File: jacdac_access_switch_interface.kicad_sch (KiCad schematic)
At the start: 23 parts

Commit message: v1.3 started, board outline complete
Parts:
- removed U: (no value), symbol Jacdac:jacdac_hole_GND_MH2A
- removed U: (no value), symbol Jacdac:jacdac_hole_GND_MH2B
- removed U: (no value), symbol Device:R
- added MH: jacdac_hole_GND_MH2, KittenBot:jacdac_hole_GND2, symbol Jacdac:jacdac_hole_GND_MH2
- added MH: jacdac_hole_GND_MH4, Kittenbot_Connector_Jacdac:jacdac_hole_GNDB, symbol Jacdac:jacdac_hole_GND_MH4
- added U (x2): (no value), symbol Device:R
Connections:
- net GND: now also MH.MH2A, MH.MH2B
- net at U.1: now also U.1
- net SWITCH renamed SWITCH1
- net SWITCH1: now also U.2
- new net: U.1, U.2
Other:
- moved on the sheet: U

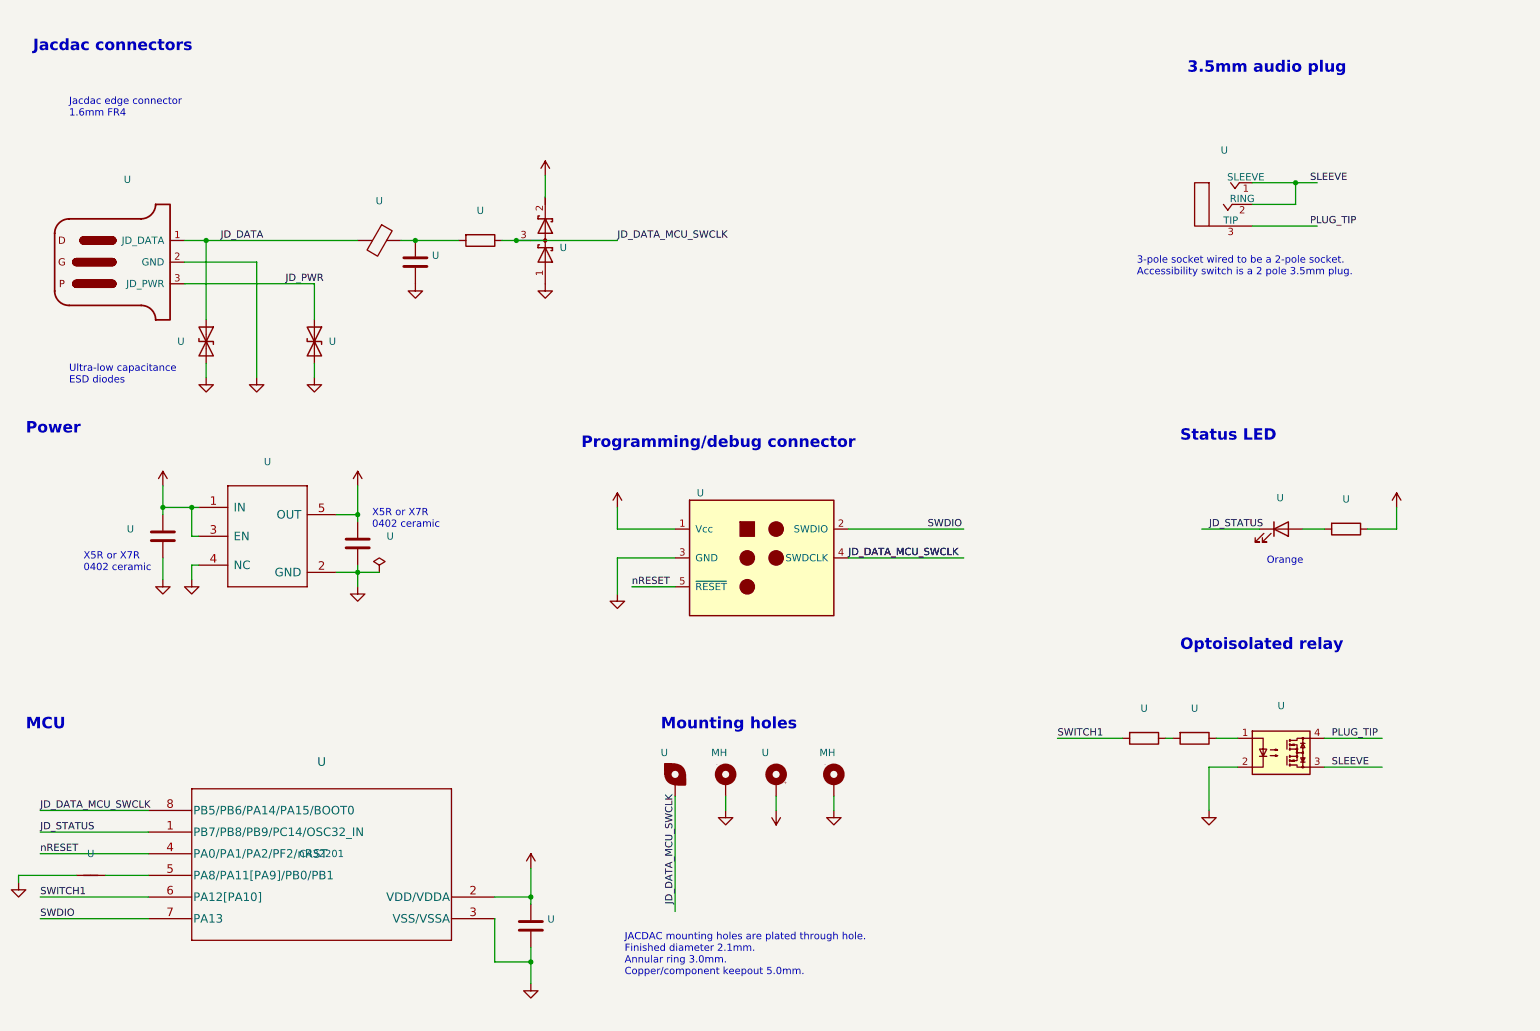
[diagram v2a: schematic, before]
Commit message: Replaced 3.5mm plug with 2x3.5mm sockets on schematic
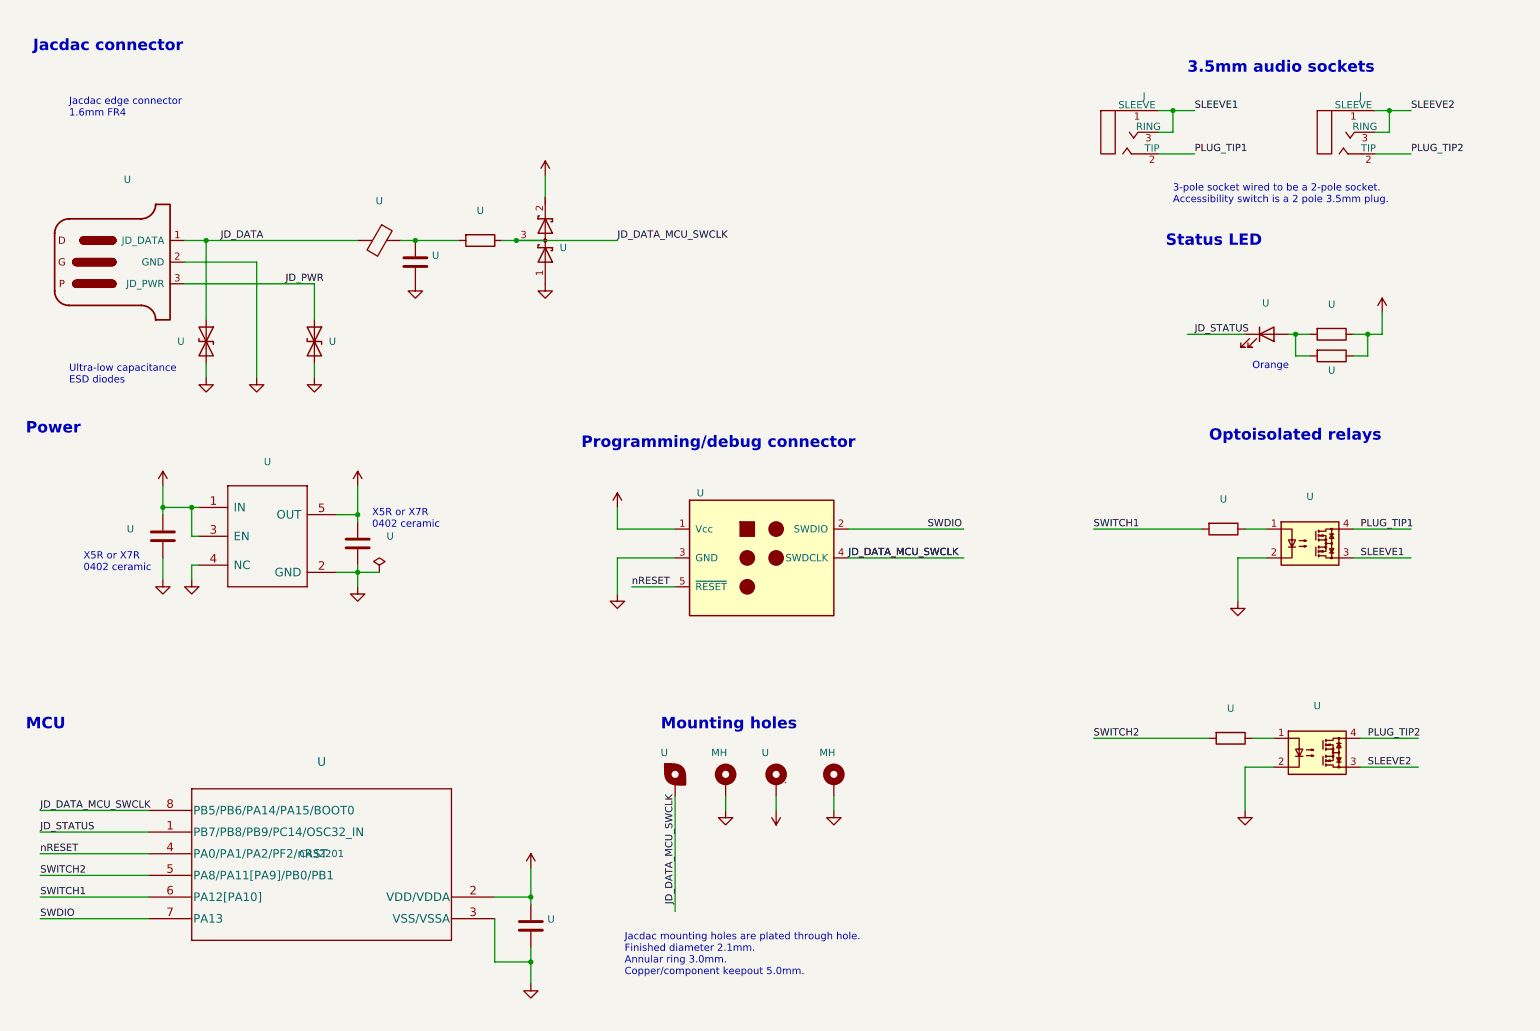
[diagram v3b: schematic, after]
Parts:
- removed U: (no value), symbol jacdac_access_switch_interface:54-00036_audio_plug
- removed U: (no value), symbol Device:NetTie_2
- removed U: (no value), symbol Device:R
- added J (x2): jack_3.5_pj313d, jacdac_access_switch_interface:jack_3.5_pj313d_smt, symbol jacdac_access_switch_interface:jack_3.5_pj313d
- added U (x2): (no value), symbol Device:R
- added U: (no value), symbol jacdac_access_switch_interface:AQY282
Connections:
- net +3V3: now also U.1
- net GND: now also U.2
- net SWITCH1: now also U.2
- net at U.2, U.2 (A): now also U.2
- net SWITCH2: now reaches U.5 (PA8/PA11[PA9]/PB0/PB1)
- net SWITCH2: now also U.2
- net PLUG_TIP renamed PLUG_TIP1
- net PLUG_TIP1: now also J.2 (TIP)
- net SLEEVE renamed SLEEVE1
- net SLEEVE1: now also J.1 (SLEEVE), J.3 (RING)
- new net: U.1, U.1
- new net PLUG_TIP2: J.2 (TIP), U.4
- new net SLEEVE2: J.1 (SLEEVE), J.3 (RING), U.3
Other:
- note added: "3.5mm audio sockets"
- note added: "Jacdac connector"
- note added: "Jacdac mounting holes are plated through hole. Finished diameter 2.1mm. Annular ring 3.0mm. Copper/component keepout 5.0mm."
- note added: "Optoisolated relays"
- note removed: "3.5mm audio plug"
- note removed: "JACDAC mounting holes are plated through hole. Finished diameter 2.1mm. Annular ring 3.0mm. Copper/component keepout 5.0mm."
- note removed: "Jacdac connectors"
- note removed: "Optoisolated relay"
- moved on the sheet: U

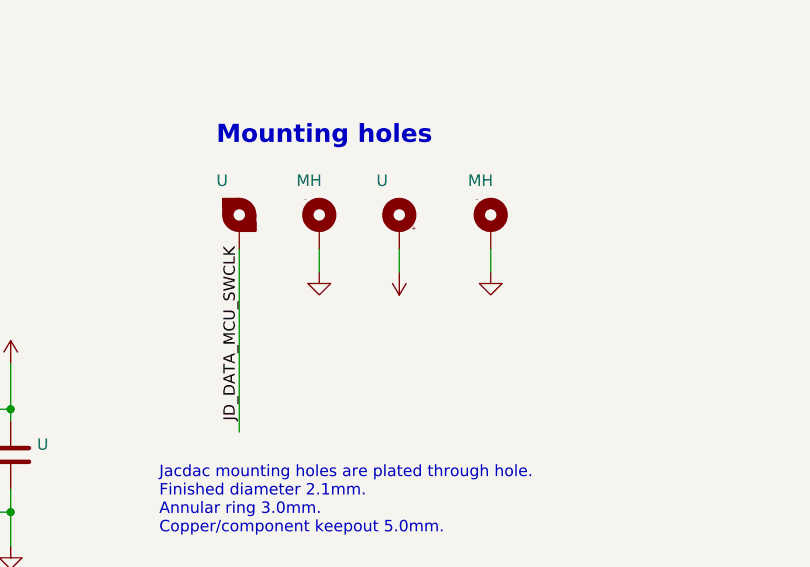
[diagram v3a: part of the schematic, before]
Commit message: Component placement for 30x30 board
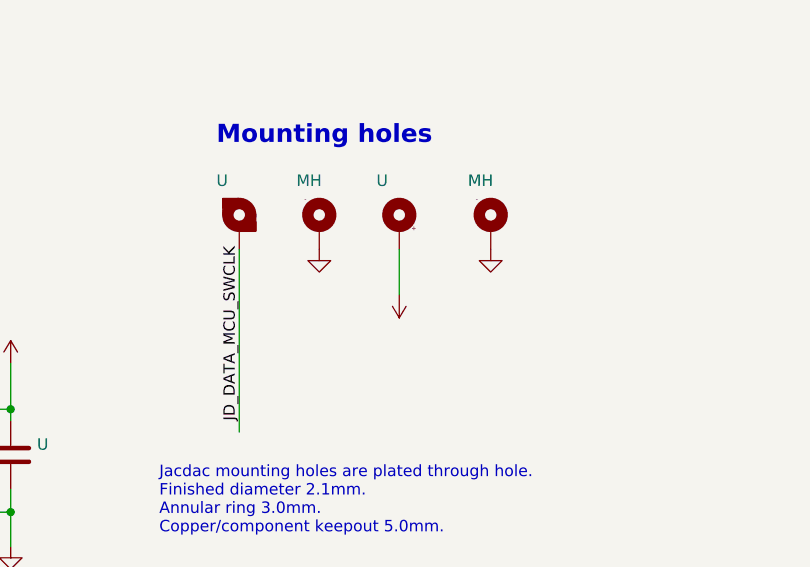
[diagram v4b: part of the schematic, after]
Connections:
- net GND: now also MH.MH2, MH.MH4; no longer MH.MH2A, MH.MH2B
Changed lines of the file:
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@@
-    (stroke (width 0) (type default))
-  )
-  (wire (pts (xy 139.7 151.13) (xy 139.7 153.67))
     (stroke (width 0) (type default))
   )
@@
     (stroke (width 0) (type default))
   )
+  (wire (pts (xy 148.59 151.13) (xy 148.59 156.21))
+    (stroke (width 0) (type default))
+  )
   (wire (pts (xy 256.54 30.48) (xy 256.54 34.29))
     (stroke (width 0) (type default))
@@
     (stroke (width 0) (type default))
   )
-  (wire (pts (xy 148.59 151.13) (xy 148.59 153.67))
-    (stroke (width 0) (type default))
-  )
   (wire (pts (xy 44.45 57.15) (xy 57.15 57.15))
     (stroke (width 0) (type default))
@@
   )
   (wire (pts (xy 46.99 105.41) (xy 45.72 105.41))
-    (stroke (width 0) (type default))
-  )
-  (wire (pts (xy 158.75 151.13) (xy 158.75 153.67))
     (stroke (width 0) (type default))
   )
@@
     (pin "MH3")
   )
-  (symbol (lib_id "power:GND") (at 139.7 153.67 0) (unit 1)
-    (in_bom yes) (on_board yes)
-    (default_instance (reference "U") (unit 1) (value "") (footprint ""))
-    (property "Reference" "U" (id 0) (at 139.7 160.02 0)
-      (effects (font (size 1.27 1.27)) hide)
-    )
-    (property "Value" "" (id 1) (at 139.827 158.0642 0)
-      (effects (font (size 1.27 1.27)))
-    )
-    (property "Footprint" "" (id 2) (at 139.7 153.67 0)
-      (effects (font (size 1.27 1.27)) hide)
-    )
-    (property "Datasheet" "" (id 3) (at 139.7 153.67 0)
-      (effects (font (size 1.27 1.27)) hide)
-    )
-    (pin "1")
-  )
-  (symbol (lib_id "power:GND") (at 158.75 153.67 0) (unit 1)
-    (in_bom yes) (on_board yes)
-    (default_instance (reference "U") (unit 1) (value "") (footprint ""))
-    (property "Reference" "U" (id 0) (at 158.75 160.02 0)
-      (effects (font (size 1.27 1.27)) hide)
-    )
-    (property "Value" "" (id 1) (at 158.877 158.0642 0)
-      (effects (font (size 1.27 1.27)))
-    )
-    (property "Footprint" "" (id 2) (at 158.75 153.67 0)
-      (effects (font (size 1.27 1.27)) hide)
-    )
-    (property "Datasheet" "" (id 3) (at 158.75 153.67 0)
+  (symbol (lib_id "power:GND") (at 139.7 151.13 0) (unit 1)
+    (in_bom yes) (on_board yes)
+    (default_instance (reference "U") (unit 1) (value "") (footprint ""))
+    (property "Reference" "U" (id 0) (at 139.7 157.48 0)
+      (effects (font (size 1.27 1.27)) hide)
+    )
+    (property "Value" "" (id 1) (at 139.827 155.5242 0)
+      (effects (font (size 1.27 1.27)))
+    )
+    (property "Footprint" "" (id 2) (at 139.7 151.13 0)
+      (effects (font (size 1.27 1.27)) hide)
+    )
+    (property "Datasheet" "" (id 3) (at 139.7 151.13 0)
+      (effects (font (size 1.27 1.27)) hide)
+    )
+    (pin "1")
+  )
+  (symbol (lib_id "power:GND") (at 158.75 151.13 0) (unit 1)
+    (in_bom yes) (on_board yes)
+    (default_instance (reference "U") (unit 1) (value "") (footprint ""))
+    (property "Reference" "U" (id 0) (at 158.75 157.48 0)
+      (effects (font (size 1.27 1.27)) hide)
+    )
+    (property "Value" "" (id 1) (at 158.877 155.5242 0)
+      (effects (font (size 1.27 1.27)))
+    )
+    (property "Footprint" "" (id 2) (at 158.75 151.13 0)
+      (effects (font (size 1.27 1.27)) hide)
+    )
+    (property "Datasheet" "" (id 3) (at 158.75 151.13 0)
       (effects (font (size 1.27 1.27)) hide)
     )
@@
     (pin "2")
   )
-  (symbol (lib_id "Jacdac:jacdac_PWR") (at 148.59 153.67 180) (unit 1)
-    (in_bom yes) (on_board yes)
-    (default_instance (reference "U") (unit 1) (value "") (footprint ""))
-    (property "Reference" "U" (id 0) (at 148.59 149.86 0)
-      (effects (font (size 1.27 1.27)) hide)
-    )
-    (property "Value" "" (id 1) (at 152.4 151.13 90)
-      (effects (font (size 1.27 1.27)))
-    )
-    (property "Footprint" "" (id 2) (at 148.59 153.67 0)
-      (effects (font (size 1.27 1.27)) hide)
-    )
-    (property "Datasheet" "" (id 3) (at 148.59 153.67 0)
+  (symbol (lib_id "Jacdac:jacdac_PWR") (at 148.59 156.21 180) (unit 1)
+    (in_bom yes) (on_board yes)
+    (default_instance (reference "U") (unit 1) (value "") (footprint ""))
+    (property "Reference" "U" (id 0) (at 148.59 152.4 0)
+      (effects (font (size 1.27 1.27)) hide)
+    )
+    (property "Value" "" (id 1) (at 152.4 153.67 90)
+      (effects (font (size 1.27 1.27)))
+    )
+    (property "Footprint" "" (id 2) (at 148.59 156.21 0)
+      (effects (font (size 1.27 1.27)) hide)
+    )
+    (property "Datasheet" "" (id 3) (at 148.59 156.21 0)
       (effects (font (size 1.27 1.27)) hide)
     )
@@
       (effects (font (size 0 0)) hide)
     )
-    (pin "MH2A")
+    (pin "MH2")
   )
   (symbol (lib_id "Device:R") (at 228.6 140.97 270) (unit 1)
@@
       (effects (font (size 0 0)) hide)
     )
-    (pin "MH2B")
+    (pin "MH4")
   )
   (symbol (lib_id "Device:R") (at 246.38 73.66 270) (unit 1)
@@
       (reference "#PWR0101") (unit 1) (value "GND") (footprint "")
     )
+    (path "/00000000-0000-0000-0000-0000610c4bd1"
+      (reference "#PWR0102") (unit 1) (value "+3V3") (footprint "")
+    )
+    (path "/00000000-0000-0000-0000-0000610d1289"
+      (reference "#PWR0103") (unit 1) (value "GND") (footprint "")
+    )
+    (path "/00000000-0000-0000-0000-000060fcc632"
+      (reference "#PWR0104") (unit 1) (value "+3V3") (footprint "")
+    )
+    (path "/00000000-0000-0000-0000-000060fae8e6"
+      (reference "#PWR0105") (unit 1) (value "jacdac_PWR") (footprint "")
+    )
     (path "/00000000-0000-0000-0000-000060fae87e"
-      (reference "#PWR0102") (unit 1) (value "GND") (footprint "")
-    )
-    (path "/00000000-0000-0000-0000-000060fcc632"
-      (reference "#PWR0103") (unit 1) (value "+3V3") (footprint "")
+      (reference "#PWR0106") (unit 1) (value "GND") (footprint "")
     )
     (path "/00000000-0000-0000-0000-000060fae878"
-      (reference "#PWR0104") (unit 1) (value "GND") (footprint "")
-    )
-    (path "/00000000-0000-0000-0000-0000610c4bd1"
-      (reference "#PWR0105") (unit 1) (value "+3V3") (footprint "")
-    )
-    (path "/00000000-0000-0000-0000-000060fae8e6"
-      (reference "#PWR0106") (unit 1) (value "jacdac_PWR") (footprint "")
-    )
-    (path "/00000000-0000-0000-0000-0000610d1289"
       (reference "#PWR0107") (unit 1) (value "GND") (footprint "")
     )
+    (path "/00000000-0000-0000-0000-000060fce0f1"
+      (reference "#PWR0108") (unit 1) (value "+3V3") (footprint "")
+    )
+    (path "/00000000-0000-0000-0000-000060fae843"
+      (reference "#PWR0109") (unit 1) (value "GND") (footprint "")
+    )
+    (path "/00000000-0000-0000-0000-000060fdc13c"
+      (reference "#PWR0110") (unit 1) (value "GND") (footprint "")
+    )
+    (path "/00000000-0000-0000-0000-000060fdc16a"
+      (reference "#PWR0111") (unit 1) (value "GND") (footprint "")
+    )
+    (path "/00000000-0000-0000-0000-000060fdc152"
+      (reference "#PWR0112") (unit 1) (value "GND") (footprint "")
+    )
+    (path "/00000000-0000-0000-0000-000061096369"
+      (reference "#PWR0113") (unit 1) (value "+3V3") (footprint "")
+    )
+    (path "/00000000-0000-0000-0000-000060fd5605"
+      (reference "#PWR0114") (unit 1) (value "GND") (footprint "")
+    )
     (path "/00000000-0000-0000-0000-000060fd6a60"
-      (reference "#PWR0108") (unit 1) (value "GND") (footprint "")
-    )
-    (path "/00000000-0000-0000-0000-000060fd5605"
-      (reference "#PWR0109") (unit 1) (value "GND") (footprint "")
+      (reference "#PWR0115") (unit 1) (value "GND") (footprint "")
     )
     (path "/00000000-0000-0000-0000-00006117a28c"
-      (reference "#PWR0110") (unit 1) (value "GND") (footprint "")
+      (reference "#PWR0116") (unit 1) (value "GND") (footprint "")
+    )
+    (path "/00000000-0000-0000-0000-000062264deb"
+      (reference "#PWR0117") (unit 1) (value "GND") (footprint "")
+    )
+    (path "/6726c9b8-874a-4f97-bf80-c9b52c702e8f"
+      (reference "#PWR0118") (unit 1) (value "GND") (footprint "")
+    )
+    (path "/00000000-0000-0000-0000-000060fae854"
+      (reference "#PWR0119") (unit 1) (value "GND") (footprint "")
+    )
+    (path "/00000000-0000-0000-0000-000060fae85a"
+      (reference "#PWR0120") (unit 1) (value "+3V3") (footprint "")
     )
     (path "/00000000-0000-0000-0000-000060fd6e61"
-      (reference "#PWR0111") (unit 1) (value "JD_PWR") (footprint "")
-    )
-    (path "/00000000-0000-0000-0000-000060fdc13c"
-      (reference "#PWR0112") (unit 1) (value "GND") (footprint "")
-    )
-    (path "/00000000-0000-0000-0000-000060fdc152"
-      (reference "#PWR0113") (unit 1) (value "GND") (footprint "")
-    )
-    (path "/00000000-0000-0000-0000-000060fdc16a"
-      (reference "#PWR0114") (unit 1) (value "GND") (footprint "")
-    )
-    (path "/00000000-0000-0000-0000-000061096369"
-      (reference "#PWR0115") (unit 1) (value "+3V3") (footprint "")
-    )
-    (path "/00000000-0000-0000-0000-000060fce0f1"
-      (reference "#PWR0116") (unit 1) (value "+3V3") (footprint "")
-    )
-    (path "/00000000-0000-0000-0000-000060fae854"
-      (reference "#PWR0117") (unit 1) (value "GND") (footprint "")
-    )
-    (path "/00000000-0000-0000-0000-000060fae85a"
-      (reference "#PWR0118") (unit 1) (value "+3V3") (footprint "")
-    )
-    (path "/00000000-0000-0000-0000-000060fae843"
-      (reference "#PWR0119") (unit 1) (value "GND") (footprint "")
-    )
-    (path "/6726c9b8-874a-4f97-bf80-c9b52c702e8f"
-      (reference "#PWR0120") (unit 1) (value "GND") (footprint "")
-    )
-    (path "/00000000-0000-0000-0000-000062264deb"
-      (reference "#PWR0121") (unit 1) (value "GND") (footprint "")
+      (reference "#PWR0121") (unit 1) (value "JD_PWR") (footprint "")
     )
     (path "/00000000-0000-0000-0000-000060fd5ec1"

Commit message: Setting up v1.5, combined input-output
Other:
- title: Jacdac access switch output -> Jacdac access switch interface
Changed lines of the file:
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@@
   (paper "A4")
   (title_block
-    (title "Jacdac access switch output")
+    (title "Jacdac access switch interface")
     (date "2022-01-07")
-    (rev "v1.4")
+    (rev "v1.5")
     (comment 3 "Licence: Attribution 4.0 International (CC BY 4.0)")
     (comment 4 "Matthew Oppenheim")
